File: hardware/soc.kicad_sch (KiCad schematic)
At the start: 1 part, among them U4 MPFS025T-FCVG484E

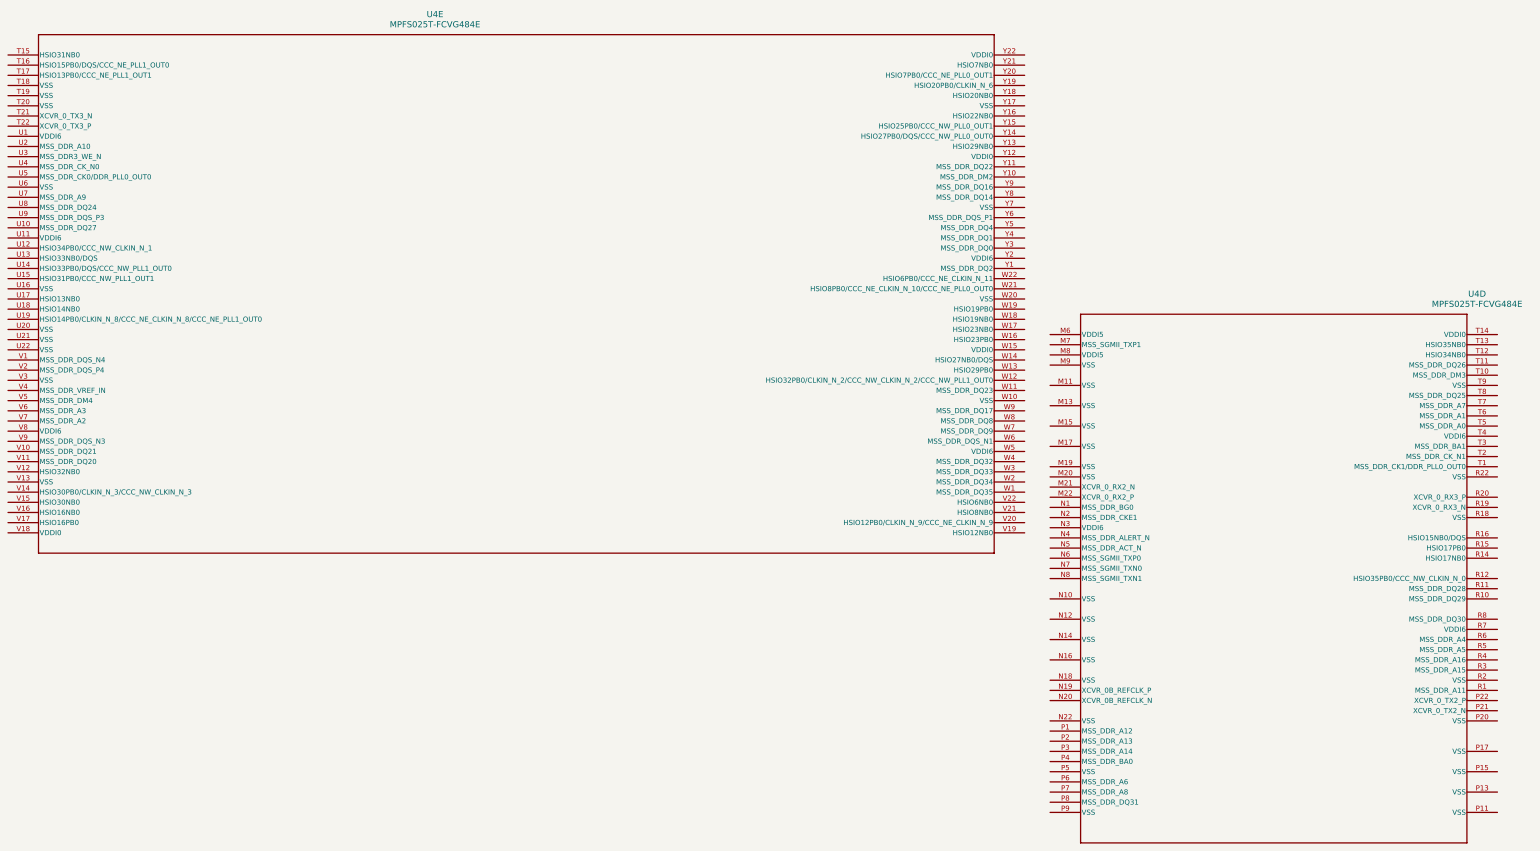
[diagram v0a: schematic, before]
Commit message: update FPGA banks schematics
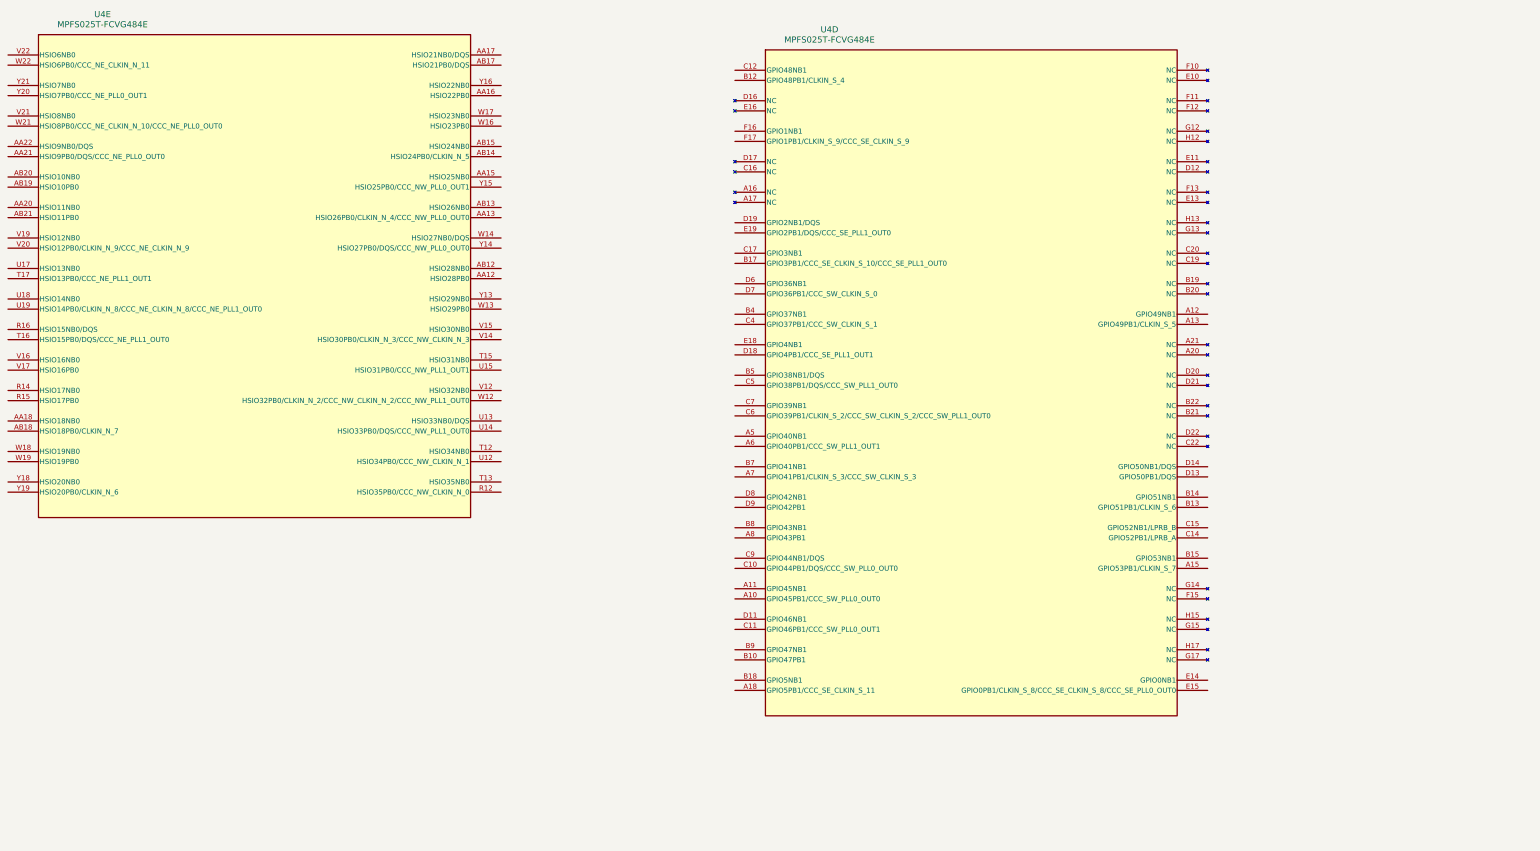
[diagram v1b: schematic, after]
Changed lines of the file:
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@@
 		(fields_autoplaced yes)
 		(property "Reference" "U4"
-			(at 137.16 21.59 0)
+			(at 54.102 21.59 0)
 			(show_name no)
 			(do_not_autoplace no)
@@
 		)
 		(property "Value" "MPFS025T-FCVG484E"
-			(at 137.16 24.13 0)
+			(at 54.102 24.13 0)
 			(show_name no)
 			(do_not_autoplace no)
@@
 			)
 			(project "RO-Instrument"
+				(path "/8fd513a2-d037-490f-a8ba-53c34aac8915"
+					(reference "U4")
+					(unit 5)
+				)
+			)
+			(project ""
 				(path "/c583dc71-b62b-403e-8742-2886e1d142c2"
 					(reference "U4")
@@
 	(symbol
 		(lib_id "payload-sym:MPFS025T-FCVG484E")
-		(at 290.83 101.6 0)
+		(at 212.09 35.56 0)
 		(unit 4)
 		(body_style 1)
@@
 		(fields_autoplaced yes)
 		(property "Reference" "U4"
-			(at 397.51 91.44 0)
+			(at 235.712 25.4 0)
 			(show_name no)
 			(do_not_autoplace no)
@@
 		)
 		(property "Value" "MPFS025T-FCVG484E"
-			(at 397.51 93.98 0)
+			(at 235.712 27.94 0)
 			(show_name no)
 			(do_not_autoplace no)
@@
 		)
 		(property "Footprint" "MPFS250T/MPFS160T/MPFS095T/MPFS025T-FCVG484_MCH"
-			(at 290.83 101.6 0)
+			(at 212.09 35.56 0)
 			(hide yes)
 			(show_name no)
@@
 		)
 		(property "Datasheet" "MPFS025T-FCVG484E"
-			(at 290.83 101.6 0)
+			(at 212.09 35.56 0)
 			(hide yes)
 			(show_name no)
@@
 		)
 		(property "Description" ""
-			(at 290.83 101.6 0)
+			(at 212.09 35.56 0)
 			(hide yes)
 			(show_name no)
@@
 			)
 			(project "RO-Instrument"
+				(path "/8fd513a2-d037-490f-a8ba-53c34aac8915"
+					(reference "U4")
+					(unit 4)
+				)
+			)
+			(project ""
 				(path "/c583dc71-b62b-403e-8742-2886e1d142c2"
 					(reference "U4")
